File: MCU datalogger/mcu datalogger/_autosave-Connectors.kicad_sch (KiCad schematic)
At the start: 4 parts, among them J1 Conn_01x04_Pin, J2 Conn_01x04_Pin, J3 Conn_01x09_Pin, J4 Conn_02x03_Odd_Even

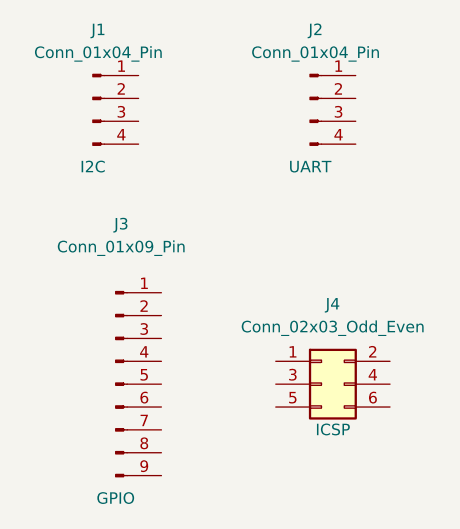
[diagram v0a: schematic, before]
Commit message: Added 2 more resitors and assembled the symbols accordingly.
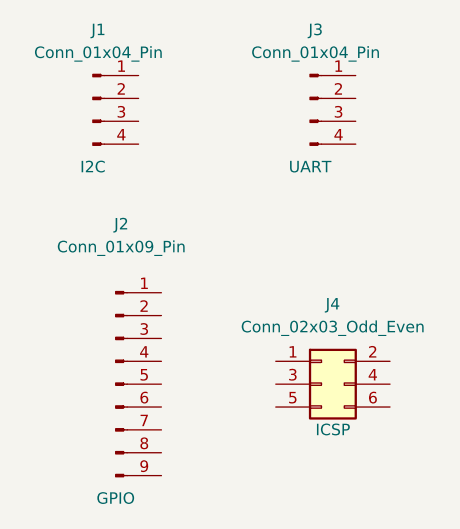
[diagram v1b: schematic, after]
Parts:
- renumbered J3 to J2, J2 to J3
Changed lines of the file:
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@@
   (symbol (lib_id "Connector:Conn_01x04_Pin") (at 149.86 68.58 0) (unit 1)
     (in_bom yes) (on_board yes) (dnp no)
-    (property "Reference" "J2" (at 150.495 60.96 0)
+    (property "Reference" "J3" (at 150.495 60.96 0)
       (effects (font (size 1.27 1.27)))
     )
@@
       (project "mcu datalogger"
         (path "/2fe2db89-a042-4e27-af2e-c9f9875d3196/6cae5f43-d748-41f5-bb24-6b82ed1e1359"
-          (reference "J2") (unit 1)
+          (reference "J3") (unit 1)
         )
       )
@@
   (symbol (lib_id "Connector:Conn_01x09_Pin") (at 128.27 100.33 0) (unit 1)
     (in_bom yes) (on_board yes) (dnp no)
-    (property "Reference" "J3" (at 128.905 82.55 0)
+    (property "Reference" "J2" (at 128.905 82.55 0)
       (effects (font (size 1.27 1.27)))
     )
@@
       (project "mcu datalogger"
         (path "/2fe2db89-a042-4e27-af2e-c9f9875d3196/6cae5f43-d748-41f5-bb24-6b82ed1e1359"
-          (reference "J3") (unit 1)
+          (reference "J2") (unit 1)
         )
       )
